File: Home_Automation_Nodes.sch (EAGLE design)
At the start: 22 parts, among them J2 Relay Connector, J3 Current Sensor, T1 2N2222, T2 2N2222, T3 2N2222, T4 2N2222

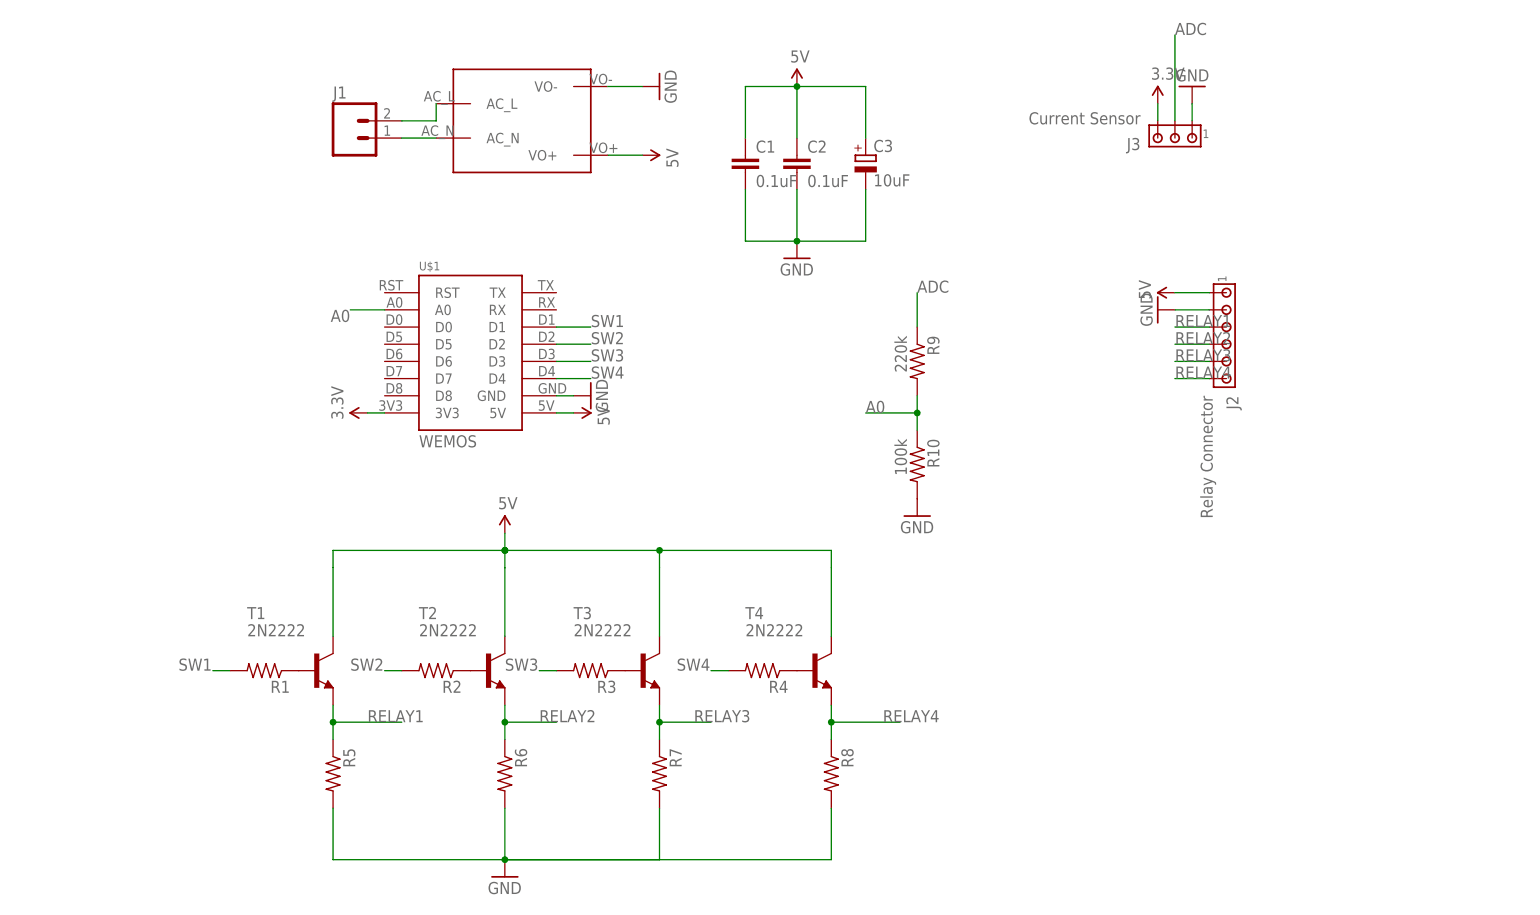
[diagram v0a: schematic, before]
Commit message: Initial Commit for 4 way switching configuration
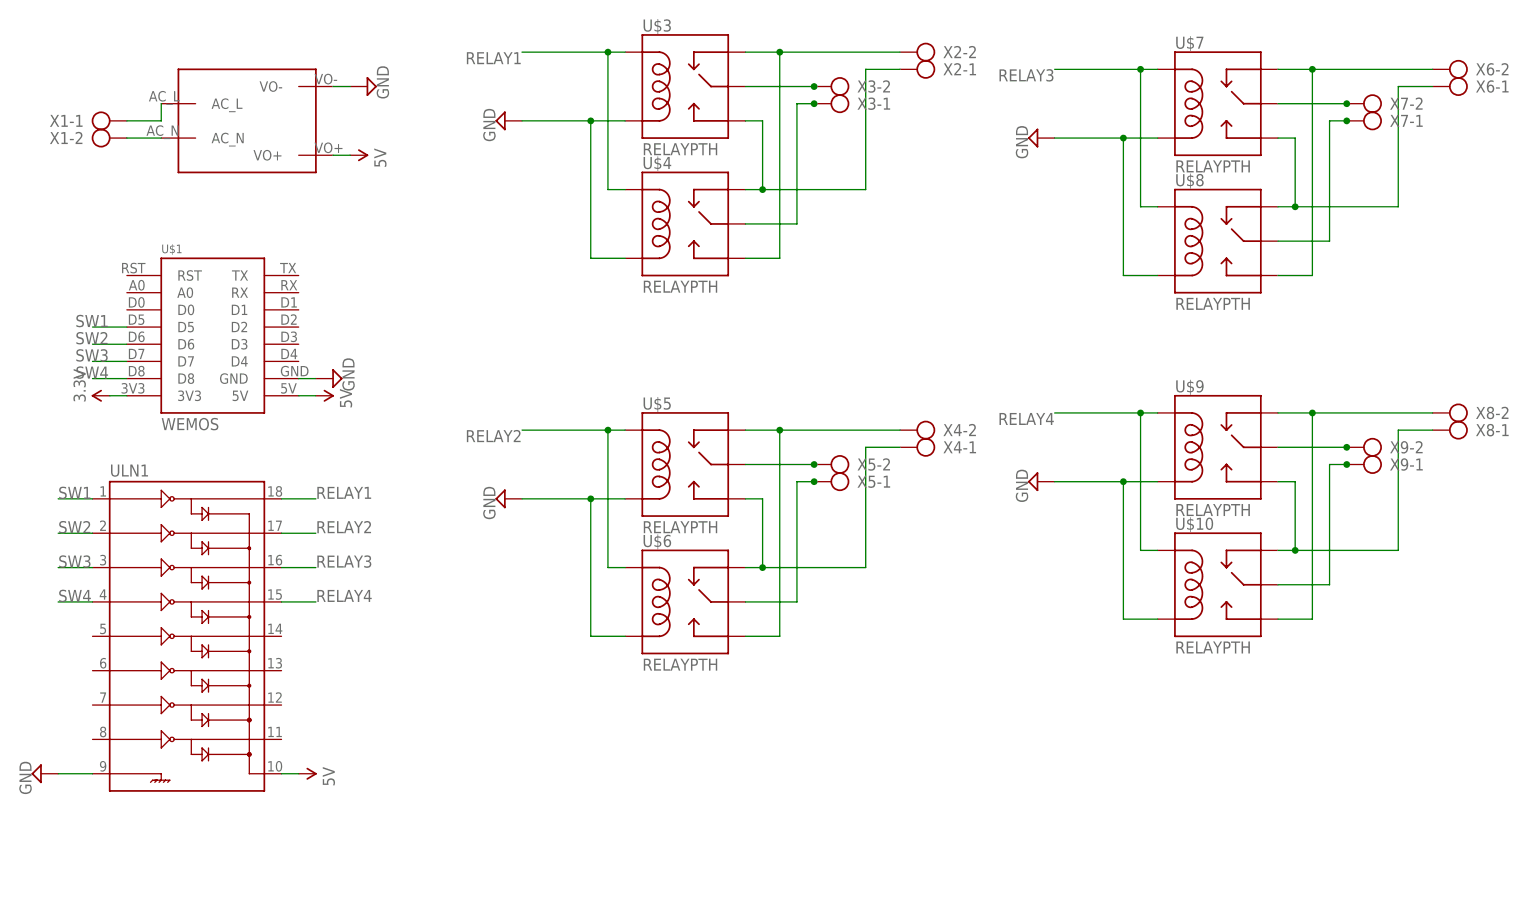
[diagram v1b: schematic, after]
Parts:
- removed C1, C2: 0.1uF, rcl:C-EU025-025X050
- removed C3: 10uF, rcl:CPOL-EUE2.5-6
- removed J1: (no value), SparkFun-Connectors:M025MM
- removed J2: Relay Connector, con-amp:MTA06-100
- removed J3: Current Sensor, con-amp:MTA03-100
- removed R1, R2, R3, R4, R5, R6, R7, R8: (no value), adafruit:R-US_0207/10
- removed R10: 100k, adafruit:R-US_0207/10
- removed R9: 220k, adafruit:R-US_0207/10
- removed T1, T2, T3, T4: 2N2222, adafruit:2N2222
- added U$10, U$3, U$4, U$5, U$6, U$7, U$8, U$9: RELAYPTH, SRD-05VDC-SL-C:RELAYPTH
- added ULN1: (no value), SparkFun-PowerIC:ULN2803DIP
- added X1, X2, X3, X4, X5, X6, X7, X8, X9: (no value), con-ptr500:AK300/2
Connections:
- removed net A0: R10.1, R9.2, U$1.A0
- removed net ADC: J3.2, R9.1
- removed net N$3: R1.1, T1.B
- removed net N$4: R2.1, T2.B
- new net N$10: U$4.SWCOMMON, X3-1.KL
- new net N$11: U$5.SWOPEN, U$6.SWCLOSE, X4-1.KL
- new net N$12: U$5.SWCLOSE, U$6.SWOPEN, X4-2.KL
- new net N$17: U$5.SWCOMMON, X5-2.KL
- new net N$18: U$6.SWCOMMON, X5-1.KL
- new net N$19: U$7.SWOPEN, U$8.SWCLOSE, X6-1.KL
- new net N$20: U$7.SWCLOSE, U$8.SWOPEN, X6-2.KL
- new net N$23: U$7.SWCOMMON, X7-2.KL
- new net N$24: U$8.SWCOMMON, X7-1.KL
- new net N$25: U$10.SWCLOSE, U$9.SWOPEN, X8-1.KL
- new net N$26: U$10.SWOPEN, U$9.SWCLOSE, X8-2.KL
- new net N$29: U$9.SWCOMMON, X9-2.KL
- new net N$30: U$10.SWCOMMON, X9-1.KL
- new net N$9: U$3.SWCOMMON, X3-2.KL
- net 3.3V: no longer J3.3
- net 5V: now also ULN1.10; no longer C1.1, C2.1, C3.+, J2.1, T1.C, T2.C, T3.C, T4.C
- net GND: now also U$10.COIL0, U$3.COIL0, U$4.COIL0, U$5.COIL0, U$6.COIL0, U$7.COIL0, U$8.COIL0, U$9.COIL0, ULN1.9; no longer C1.2, C2.2, C3.-, J2.2, J3.1, R10.2, R5.2, R6.2, R7.2, R8.2
- net N$1: now also X1-2.KL; no longer J1.1
- net N$2: now also X1-1.KL; no longer J1.2
- net N$5: now also U$3.SWOPEN, U$4.SWCLOSE, X2-1.KL; no longer R3.1, T3.B
- net N$6: now also U$3.SWCLOSE, U$4.SWOPEN, X2-2.KL; no longer R4.1, T4.B
- net RELAY1: now also U$3.COIL1, U$4.COIL1, ULN1.18; no longer J2.3, R5.1, T1.E
- net RELAY2: now also U$5.COIL1, U$6.COIL1, ULN1.17; no longer J2.4, R6.1, T2.E
- net RELAY3: now also U$7.COIL1, U$8.COIL1, ULN1.16; no longer J2.5, R7.1, T3.E
- net RELAY4: now also U$10.COIL1, U$9.COIL1, ULN1.15; no longer J2.6, R8.1, T4.E
- net SW1: now also U$1.D5, ULN1.1; no longer R1.2, U$1.D1
- net SW2: now also U$1.D6, ULN1.2; no longer R2.2, U$1.D2
- net SW3: now also U$1.D7, ULN1.3; no longer R3.2, U$1.D3
- net SW4: now also U$1.D8, ULN1.4; no longer R4.2, U$1.D4
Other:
- note added: "Wemos D1 Mini Sch: https://www.wemos.cc/sites/default/files/2016-09/mini_pro.pdf NodeMCU Sch: https://github.com/nodemcu/nodemcu-devkit-v1.0/blob/master/NODEMCU_DEVKIT_V1.0.PDF Relay lbr from: https://github.com/dvdnhm/Maker-Tools-Eagle-Libraries"
- note removed: "Wemos D1 Mini Sch: https://www.wemos.cc/sites/default/files/2016-09/mini_pro.pdf NodeMCU Sch: https://github.com/nodemcu/nodemcu-devkit-v1.0/blob/master/NODEMCU_DEVKIT_V1.0.PDF"
- moved on the sheet: U$1

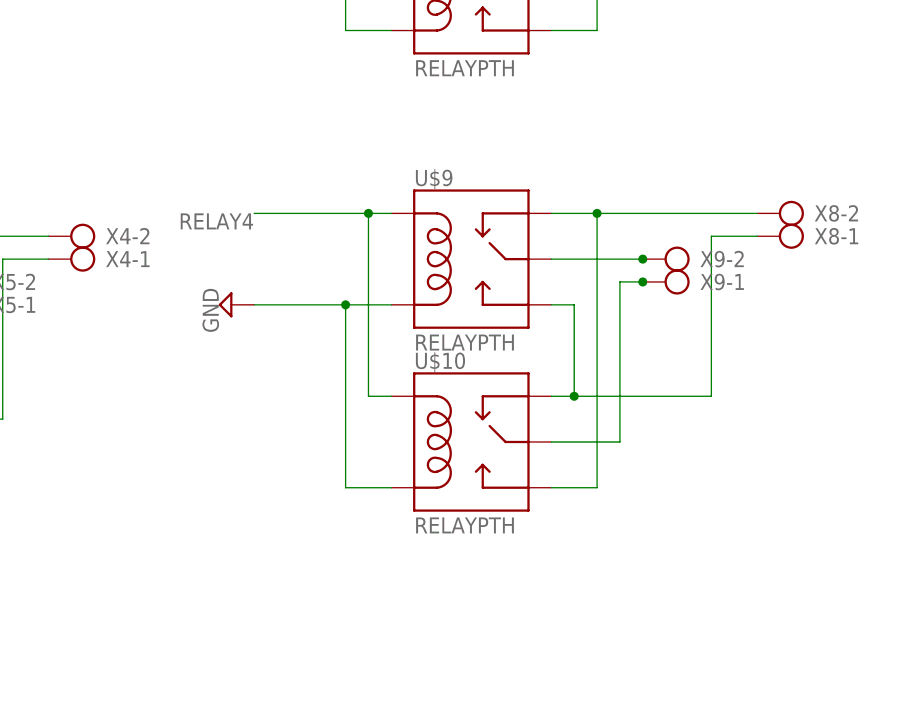
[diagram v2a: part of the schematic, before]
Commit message: Removed a set of relay. Still routing
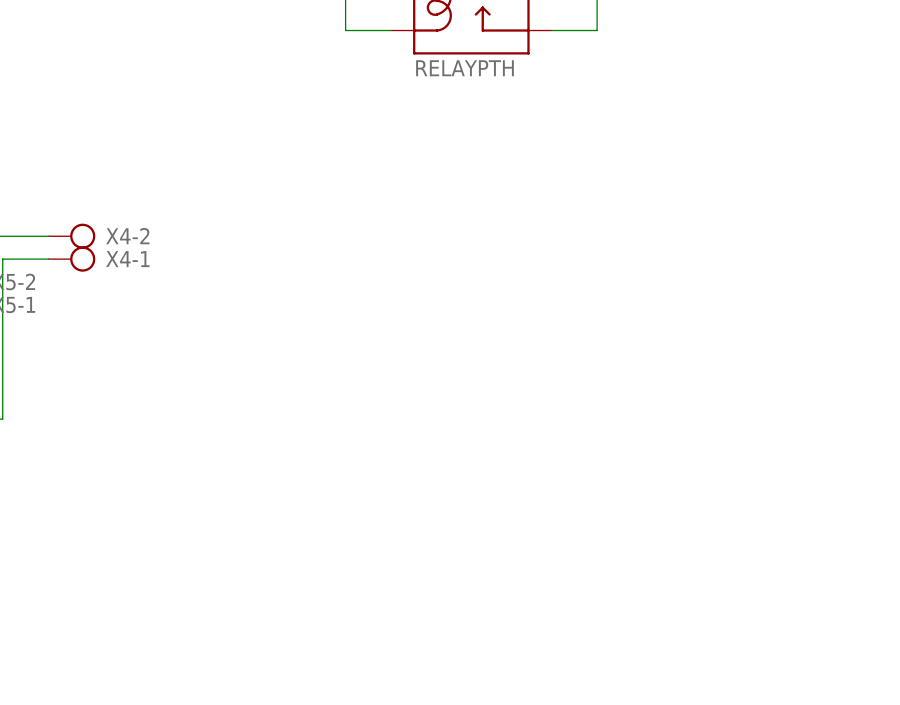
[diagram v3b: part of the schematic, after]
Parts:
- removed U$10, U$9: RELAYPTH, SRD-05VDC-SL-C:RELAYPTH
- removed X8, X9: (no value), con-ptr500:AK300/2
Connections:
- removed net N$25: U$10.SWCLOSE, U$9.SWOPEN, X8-1.KL
- removed net N$26: U$10.SWOPEN, U$9.SWCLOSE, X8-2.KL
- removed net N$29: U$9.SWCOMMON, X9-2.KL
- removed net N$30: U$10.SWCOMMON, X9-1.KL
- net GND: no longer U$10.COIL0, U$9.COIL0
- net RELAY4: no longer U$10.COIL1, U$9.COIL1
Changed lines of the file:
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@@
 <part name="X6" library="con-ptr500" deviceset="AK300/2" device=""/>
 <part name="X7" library="con-ptr500" deviceset="AK300/2" device=""/>
-<part name="U$9" library="SRD-05VDC-SL-C" deviceset="RELAY" device="PTH"/>
-<part name="U$10" library="SRD-05VDC-SL-C" deviceset="RELAY" device="PTH"/>
-<part name="X8" library="con-ptr500" deviceset="AK300/2" device=""/>
-<part name="X9" library="con-ptr500" deviceset="AK300/2" device=""/>
 <part name="SUPPLY1" library="SparkFun-Aesthetics" deviceset="5V" device=""/>
 <part name="SUPPLY3" library="SparkFun-Aesthetics" deviceset="5V" device=""/>
@@
 <part name="SUPPLY11" library="supply2" deviceset="GND" device=""/>
 <part name="SUPPLY12" library="supply2" deviceset="GND" device=""/>
-<part name="SUPPLY13" library="supply2" deviceset="GND" device=""/>
 </parts>
 <sheets>
@@
 <instance part="X7" gate="-1" x="149.86" y="124.46" rot="R180"/>
 <instance part="X7" gate="-2" x="149.86" y="127" rot="R180"/>
-<instance part="U$9" gate="G$1" x="127" y="76.2"/>
-<instance part="U$10" gate="G$1" x="127" y="55.88"/>
-<instance part="X8" gate="-1" x="162.56" y="78.74" rot="R180"/>
-<instance part="X8" gate="-2" x="162.56" y="81.28" rot="R180"/>
-<instance part="X9" gate="-1" x="149.86" y="73.66" rot="R180"/>
-<instance part="X9" gate="-2" x="149.86" y="76.2" rot="R180"/>
 <instance part="SUPPLY1" gate="G$1" x="-2.54" y="119.38" rot="R270"/>
 <instance part="SUPPLY3" gate="G$1" x="-7.62" y="83.82" rot="R270"/>
@@
 <instance part="SUPPLY11" gate="GND" x="20.32" y="124.46" rot="R270"/>
 <instance part="SUPPLY12" gate="GND" x="99.06" y="121.92" rot="R270"/>
-<instance part="SUPPLY13" gate="GND" x="99.06" y="71.12" rot="R270"/>
 </instances>
 <busses>
@@
 </segment>
 </net>
-<net name="N$25" class="0">
-<segment>
-<pinref part="U$9" gate="G$1" pin="SWOPEN"/>
-<wire x1="134.62" y1="71.12" x2="137.16" y2="71.12" width="0.1524" layer="91"/>
-<wire x1="137.16" y1="71.12" x2="137.16" y2="60.96" width="0.1524" layer="91"/>
-<pinref part="U$10" gate="G$1" pin="SWCLOSE"/>
-<wire x1="137.16" y1="60.96" x2="134.62" y2="60.96" width="0.1524" layer="91"/>
-<wire x1="137.16" y1="60.96" x2="152.4" y2="60.96" width="0.1524" layer="91"/>
-<wire x1="152.4" y1="60.96" x2="152.4" y2="78.74" width="0.1524" layer="91"/>
-<junction x="137.16" y="60.96"/>
-<wire x1="152.4" y1="78.74" x2="157.48" y2="78.74" width="0.1524" layer="91"/>
-<pinref part="X8" gate="-1" pin="KL"/>
-</segment>
-</net>
-<net name="N$26" class="0">
-<segment>
-<pinref part="U$9" gate="G$1" pin="SWCLOSE"/>
-<wire x1="134.62" y1="81.28" x2="139.7" y2="81.28" width="0.1524" layer="91"/>
-<wire x1="139.7" y1="81.28" x2="139.7" y2="50.8" width="0.1524" layer="91"/>
-<pinref part="U$10" gate="G$1" pin="SWOPEN"/>
-<wire x1="139.7" y1="50.8" x2="134.62" y2="50.8" width="0.1524" layer="91"/>
-<wire x1="139.7" y1="81.28" x2="157.48" y2="81.28" width="0.1524" layer="91"/>
-<junction x="139.7" y="81.28"/>
-<pinref part="X8" gate="-2" pin="KL"/>
-</segment>
-</net>
-<net name="N$29" class="0">
-<segment>
-<pinref part="U$9" gate="G$1" pin="SWCOMMON"/>
-<wire x1="134.62" y1="76.2" x2="144.78" y2="76.2" width="0.1524" layer="91"/>
-<pinref part="X9" gate="-2" pin="KL"/>
-<junction x="144.78" y="76.2"/>
-</segment>
-</net>
-<net name="N$30" class="0">
-<segment>
-<pinref part="U$10" gate="G$1" pin="SWCOMMON"/>
-<wire x1="134.62" y1="55.88" x2="142.24" y2="55.88" width="0.1524" layer="91"/>
-<wire x1="142.24" y1="55.88" x2="142.24" y2="73.66" width="0.1524" layer="91"/>
-<wire x1="142.24" y1="73.66" x2="144.78" y2="73.66" width="0.1524" layer="91"/>
-<pinref part="X9" gate="-1" pin="KL"/>
-<junction x="144.78" y="73.66"/>
-</segment>
-</net>
 <net name="5V" class="0">
 <segment>
@@
 </segment>
 <segment>
-<pinref part="U$9" gate="G$1" pin="COIL0"/>
-<wire x1="116.84" y1="71.12" x2="111.76" y2="71.12" width="0.1524" layer="91"/>
-<pinref part="U$10" gate="G$1" pin="COIL0"/>
-<wire x1="111.76" y1="71.12" x2="101.6" y2="71.12" width="0.1524" layer="91"/>
-<wire x1="116.84" y1="50.8" x2="111.76" y2="50.8" width="0.1524" layer="91"/>
-<wire x1="111.76" y1="50.8" x2="111.76" y2="71.12" width="0.1524" layer="91"/>
-<junction x="111.76" y="71.12"/>
-<pinref part="SUPPLY13" gate="GND" pin="GND"/>
-</segment>
-<segment>
 <pinref part="U$2" gate="G$1" pin="VO-"/>
 <pinref part="SUPPLY5" gate="GND" pin="GND"/>
@@
 <label x="-7.62" y="53.34" size="1.778" layer="95"/>
 </segment>
-<segment>
-<pinref part="U$9" gate="G$1" pin="COIL1"/>
-<wire x1="116.84" y1="81.28" x2="114.3" y2="81.28" width="0.1524" layer="91"/>
-<pinref part="U$10" gate="G$1" pin="COIL1"/>
-<wire x1="114.3" y1="81.28" x2="101.6" y2="81.28" width="0.1524" layer="91"/>
-<wire x1="116.84" y1="60.96" x2="114.3" y2="60.96" width="0.1524" layer="91"/>
-<wire x1="114.3" y1="60.96" x2="114.3" y2="81.28" width="0.1524" layer="91"/>
-<junction x="114.3" y="81.28"/>
-<label x="101.6" y="81.28" size="1.778" layer="95" rot="R180"/>
-</segment>
-</net>
+</net>

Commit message: Changes: 1. SCH: Added decoupling capacitor. Breakout for A0 and 4 digital pins 2. BRD: 100 mils spacing, 80 mils track width. Legends added
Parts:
- added C1: 0.1uF, rcl:C-EU025-025X050
- added J1: (no value), con-amp:MTA03-100
- added J2: (no value), con-amp:MTA07-100
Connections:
- removed net N$23: U$7.SWCOMMON, X7-2.KL
- removed net N$9: U$3.SWCOMMON, X3-2.KL
- new net A0: J1.2, U$1.A0
- new net D1: J2.4, U$1.D1
- new net D2: J2.5, U$1.D2
- new net D3: J2.6, U$1.D3
- new net D4: J2.7, U$1.D4
- new net N$16: U$1.RX
- new net N$3: U$3.SWCOMMON, X3-1.KL
- new net N$4: U$5.SWCOMMON, X5-1.KL
- new net N$7: U$7.SWCOMMON, X7-1.KL
- net 3.3V: now also J1.1, J2.2
- net 5V: now also C1.1, J1.3, J2.1
- net GND: now also C1.2, J2.3
- net N$10: now also X3-2.KL; no longer X3-1.KL
- net N$17: now also U$1.TX; no longer U$5.SWCOMMON, X5-2.KL
- net N$18: now also X5-2.KL; no longer X5-1.KL
- net N$24: now also X7-2.KL; no longer X7-1.KL

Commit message: Final version. Sent to Mervin for verification
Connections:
- net 5V: no longer J1.3
- net GND: now also J1.3
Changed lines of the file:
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@@
 <part name="SUPPLY6" library="SparkFun-Aesthetics" deviceset="3.3V" device=""/>
 <part name="SUPPLY13" library="supply2" deviceset="GND" device=""/>
-<part name="SUPPLY14" library="SparkFun-Aesthetics" deviceset="5V" device=""/>
 <part name="SUPPLY15" library="SparkFun-Aesthetics" deviceset="5V" device=""/>
 <part name="C1" library="rcl" deviceset="C-EU" device="025-025X050" value="0.1uF"/>
 <part name="SUPPLY16" library="SparkFun-Aesthetics" deviceset="5V" device=""/>
 <part name="SUPPLY17" library="supply2" deviceset="GND" device=""/>
+<part name="SUPPLY14" library="supply2" deviceset="GND" device=""/>
 </parts>
 <sheets>
@@
 <instance part="SUPPLY6" gate="G$1" x="127" y="71.12" rot="R180"/>
 <instance part="SUPPLY13" gate="GND" x="129.54" y="68.58"/>
-<instance part="SUPPLY14" gate="G$1" x="111.76" y="71.12" rot="R180"/>
 <instance part="SUPPLY15" gate="G$1" x="124.46" y="71.12" rot="R180"/>
 <instance part="C1" gate="G$1" x="5.08" y="109.22"/>
 <instance part="SUPPLY16" gate="G$1" x="10.16" y="114.3"/>
 <instance part="SUPPLY17" gate="GND" x="10.16" y="99.06"/>
+<instance part="SUPPLY14" gate="GND" x="111.76" y="68.58"/>
 </instances>
 <busses>
@@
 </segment>
 <segment>
-<pinref part="J1" gate="G$1" pin="3"/>
-<wire x1="111.76" y1="76.2" x2="111.76" y2="71.12" width="0.1524" layer="91"/>
-<pinref part="SUPPLY14" gate="G$1" pin="5V"/>
-</segment>
-<segment>
 <pinref part="J2" gate="G$1" pin="1"/>
 <wire x1="124.46" y1="76.2" x2="124.46" y2="71.12" width="0.1524" layer="91"/>
@@
 <junction x="10.16" y="101.6"/>
 </segment>
-</net>
+<segment>
+<pinref part="J1" gate="G$1" pin="3"/>
+<wire x1="111.76" y1="76.2" x2="111.76" y2="71.12" width="0.1524" layer="91"/>
+<pinref part="SUPPLY14" gate="GND" pin="GND"/>
+</segment>
+</net>
